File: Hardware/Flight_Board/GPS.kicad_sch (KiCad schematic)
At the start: 10 parts, among them U5 CAM-M8Q-0

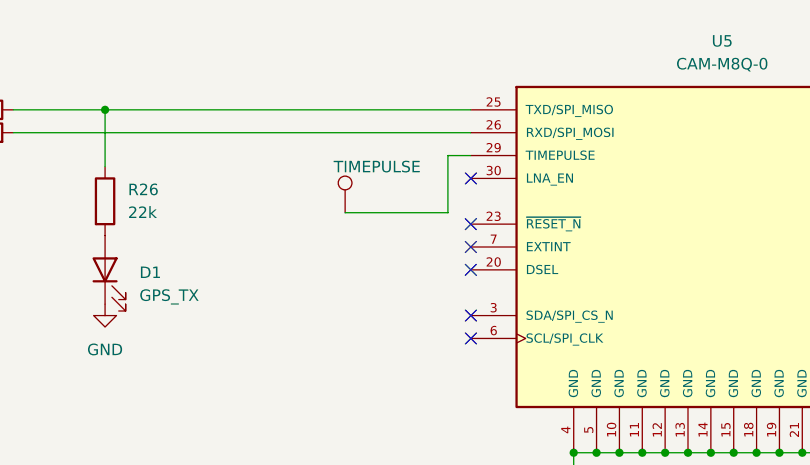
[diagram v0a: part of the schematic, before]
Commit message: fix some stuff and begin layout grouping
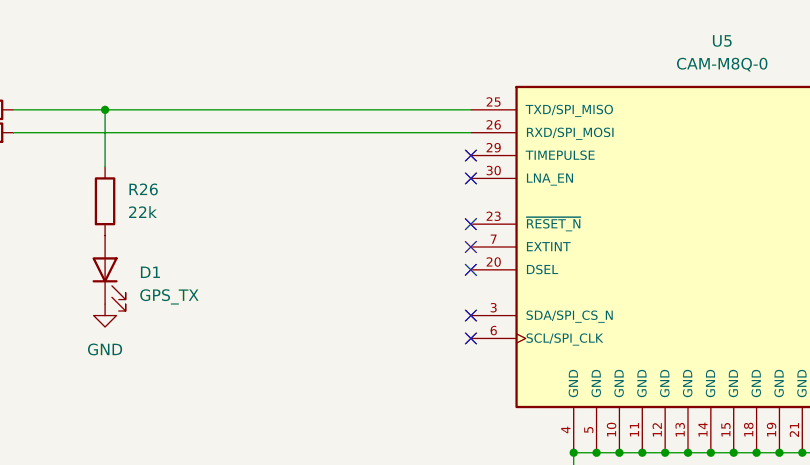
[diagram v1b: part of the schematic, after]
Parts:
- removed TP2: TIMEPULSE, TestPoint:TestPoint_THTPad_2.0x2.0mm_Drill1.0mm, symbol Connector:TestPoint
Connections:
- no-connect marks 8 -> 9
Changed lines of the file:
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@@
   (junction (at 177.8 100.33) (diameter 0) (color 0 0 0 0)
   )
+  (no_connect (at 146.05 67.31))
   (no_connect (at 146.05 77.47))
   (no_connect (at 146.05 69.85))
@@
     (stroke (width 0) (type default))
   )
-  (wire (pts (xy 132.08 73.66) (xy 143.51 73.66))
-    (stroke (width 0) (type default))
-  )
-  (wire (pts (xy 143.51 67.31) (xy 143.51 73.66))
-    (stroke (width 0) (type default))
-  )
   (wire (pts (xy 201.93 82.55) (xy 217.17 82.55))
     (stroke (width 0) (type default))
@@
   )
   (wire (pts (xy 201.93 62.23) (xy 212.09 62.23))
-    (stroke (width 0) (type default))
-  )
-  (wire (pts (xy 146.05 67.31) (xy 143.51 67.31))
     (stroke (width 0) (type default))
   )
@@
         )
       )
-    )
-  )
-  (symbol (lib_id "Connector:TestPoint") (at 132.08 73.66 0) (unit 1)
-    (in_bom yes) (on_board yes) (dnp no)
-    (property "Reference" "TP2" (at 137.16 70.358 90)
-      (effects (font (size 1.27 1.27)) hide)
-    )
-    (property "Value" "TIMEPULSE" (at 130.81 68.58 0)
-      (effects (font (size 1.27 1.27)) (justify left))
-    )
-    (property "Footprint" "TestPoint:TestPoint_THTPad_2.0x2.0mm_Drill1.0mm" (at 137.16 73.66 0)
-      (effects (font (size 1.27 1.27)) hide)
-    )
-    (property "Datasheet" "~" (at 137.16 73.66 0)
-      (effects (font (size 1.27 1.27)) hide)
-    )
-    (pin "1")
-    (instances
-      (project "Flight_Board"
-        (path "/e8eb85d5-f1ff-4500-895d-25b9ff5f6d36/bc23ea56-d50e-4ce7-856f-e38dfbe72971"
-          (reference "TP2") (unit 1)
-        )
-        (path "/e8eb85d5-f1ff-4500-895d-25b9ff5f6d36/43c0adf1-436b-4b66-9010-44cf9a79cc96"
-          (reference "TP3") (unit 1)
-        )
-        (path "/e8eb85d5-f1ff-4500-895d-25b9ff5f6d36/7c06db2a-34f5-45c0-9668-fbbbd940678c"
-          (reference "TP11") (unit 1)
-        )
-        (path "/e8eb85d5-f1ff-4500-895d-25b9ff5f6d36/52cae81a-54fe-42c0-9a19-be88b271d004"
-          (reference "TP15") (unit 1)
-        )
-      )

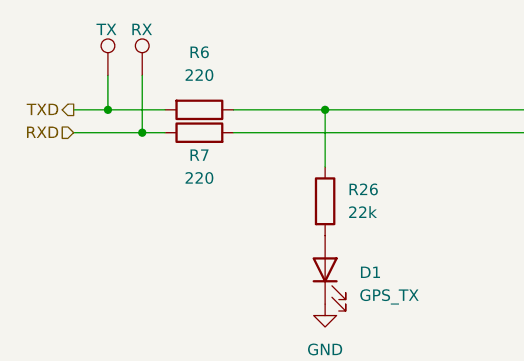
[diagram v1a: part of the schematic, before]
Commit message: initial placement on board, continue routing
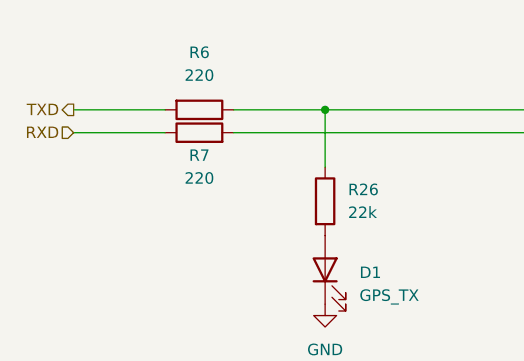
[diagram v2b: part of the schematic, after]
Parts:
- removed TP2: RX, TestPoint:TestPoint_THTPad_2.0x2.0mm_Drill1.0mm, symbol Connector:TestPoint
- removed TP2: TX, TestPoint:TestPoint_THTPad_2.0x2.0mm_Drill1.0mm, symbol Connector:TestPoint
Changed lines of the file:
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@@
 (kicad_sch (version 20230121) (generator eeschema)
   (paper "A4")
-  (junction (at 85.09 64.77) (diameter 0) (color 0 0 0 0)
-  )
   (junction (at 105.41 62.23) (diameter 0) (color 0 0 0 0)
   )
@@
   )
   (junction (at 167.64 100.33) (diameter 0) (color 0 0 0 0)
-  )
-  (junction (at 81.28 62.23) (diameter 0) (color 0 0 0 0)
   )
   (junction (at 175.26 100.33) (diameter 0) (color 0 0 0 0)
@@
     (stroke (width 0) (type default))
   )
-  (wire (pts (xy 85.09 58.42) (xy 85.09 64.77))
-    (stroke (width 0) (type default))
-  )
   (wire (pts (xy 212.09 62.23) (xy 212.09 64.77))
     (stroke (width 0) (type default))
@@
     (stroke (width 0) (type default))
   )
-  (wire (pts (xy 81.28 62.23) (xy 87.63 62.23))
-    (stroke (width 0) (type default))
-  )
   (wire (pts (xy 204.47 72.39) (xy 201.93 72.39))
     (stroke (width 0) (type default))
@@
     (stroke (width 0) (type default))
   )
-  (wire (pts (xy 77.47 64.77) (xy 85.09 64.77))
-    (stroke (width 0) (type default))
-  )
-  (wire (pts (xy 77.47 62.23) (xy 81.28 62.23))
-    (stroke (width 0) (type default))
-  )
-  (wire (pts (xy 85.09 64.77) (xy 87.63 64.77))
+  (wire (pts (xy 77.47 64.77) (xy 87.63 64.77))
+    (stroke (width 0) (type default))
+  )
+  (wire (pts (xy 77.47 62.23) (xy 87.63 62.23))
     (stroke (width 0) (type default))
   )
@@
   )
   (wire (pts (xy 160.02 100.33) (xy 162.56 100.33))
-    (stroke (width 0) (type default))
-  )
-  (wire (pts (xy 81.28 58.42) (xy 81.28 62.23))
     (stroke (width 0) (type default))
   )
@@
     )
   )
-  (symbol (lib_id "Connector:TestPoint") (at 85.09 58.42 0) (unit 1)
-    (in_bom yes) (on_board yes) (dnp no)
-    (property "Reference" "TP2" (at 90.17 55.118 90)
-      (effects (font (size 1.27 1.27)) hide)
-    )
-    (property "Value" "RX" (at 83.82 53.34 0)
-      (effects (font (size 1.27 1.27)) (justify left))
-    )
-    (property "Footprint" "TestPoint:TestPoint_THTPad_2.0x2.0mm_Drill1.0mm" (at 90.17 58.42 0)
-      (effects (font (size 1.27 1.27)) hide)
-    )
-    (property "Datasheet" "~" (at 90.17 58.42 0)
-      (effects (font (size 1.27 1.27)) hide)
-    )
-    (pin "1")
-    (instances
-      (project "Flight_Board"
-        (path "/e8eb85d5-f1ff-4500-895d-25b9ff5f6d36/bc23ea56-d50e-4ce7-856f-e38dfbe72971"
-          (reference "TP2") (unit 1)
-        )
-        (path "/e8eb85d5-f1ff-4500-895d-25b9ff5f6d36/43c0adf1-436b-4b66-9010-44cf9a79cc96"
-          (reference "TP3") (unit 1)
-        )
-        (path "/e8eb85d5-f1ff-4500-895d-25b9ff5f6d36/7c06db2a-34f5-45c0-9668-fbbbd940678c"
-          (reference "TP11") (unit 1)
-        )
-        (path "/e8eb85d5-f1ff-4500-895d-25b9ff5f6d36/52cae81a-54fe-42c0-9a19-be88b271d004"
-          (reference "TP14") (unit 1)
-        )
-      )
-    )
-  )
   (symbol (lib_id "power:GND") (at 157.48 102.87 0) (unit 1)
     (in_bom yes) (on_board yes) (dnp no) (fields_autoplaced)
@@
         )
       )
-    )
-  )
-  (symbol (lib_id "Connector:TestPoint") (at 81.28 58.42 0) (unit 1)
-    (in_bom yes) (on_board yes) (dnp no)
-    (property "Reference" "TP2" (at 86.36 55.118 90)
-      (effects (font (size 1.27 1.27)) hide)
-    )
-    (property "Value" "TX" (at 80.01 53.34 0)
-      (effects (font (size 1.27 1.27)) (justify left))
-    )
-    (property "Footprint" "TestPoint:TestPoint_THTPad_2.0x2.0mm_Drill1.0mm" (at 86.36 58.42 0)
-      (effects (font (size 1.27 1.27)) hide)
-    )
-    (property "Datasheet" "~" (at 86.36 58.42 0)
-      (effects (font (size 1.27 1.27)) hide)
-    )
-    (pin "1")
-    (instances
-      (project "Flight_Board"
-        (path "/e8eb85d5-f1ff-4500-895d-25b9ff5f6d36/bc23ea56-d50e-4ce7-856f-e38dfbe72971"
-          (reference "TP2") (unit 1)
-        )
-        (path "/e8eb85d5-f1ff-4500-895d-25b9ff5f6d36/43c0adf1-436b-4b66-9010-44cf9a79cc96"
-          (reference "TP3") (unit 1)
-        )
-        (path "/e8eb85d5-f1ff-4500-895d-25b9ff5f6d36/7c06db2a-34f5-45c0-9668-fbbbd940678c"
-          (reference "TP11") (unit 1)
-        )
-        (path "/e8eb85d5-f1ff-4500-895d-25b9ff5f6d36/52cae81a-54fe-42c0-9a19-be88b271d004"
-          (reference "TP13") (unit 1)
-        )
-      )

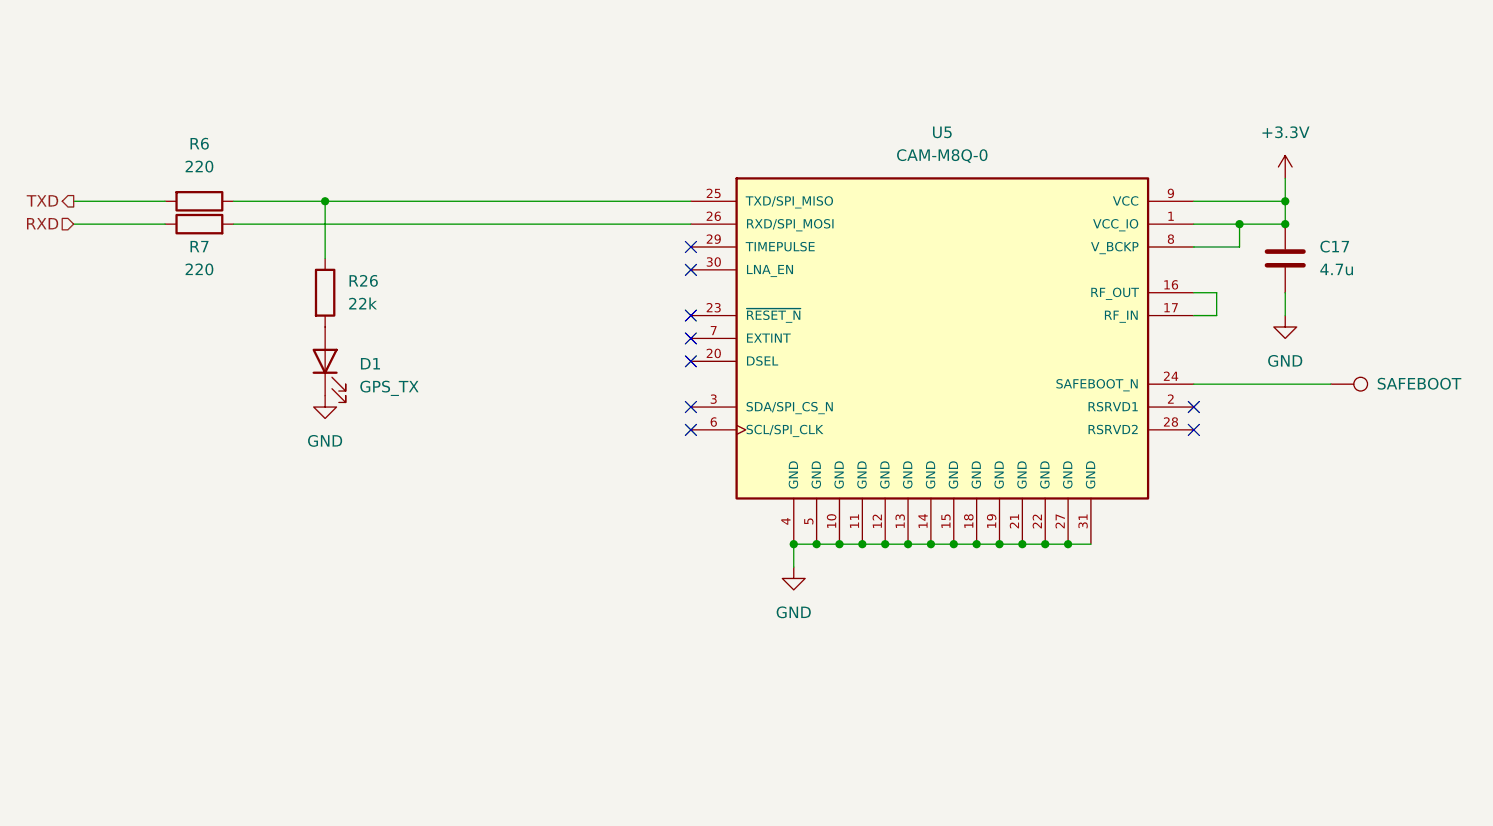
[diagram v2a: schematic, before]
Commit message: begin 4 layer board
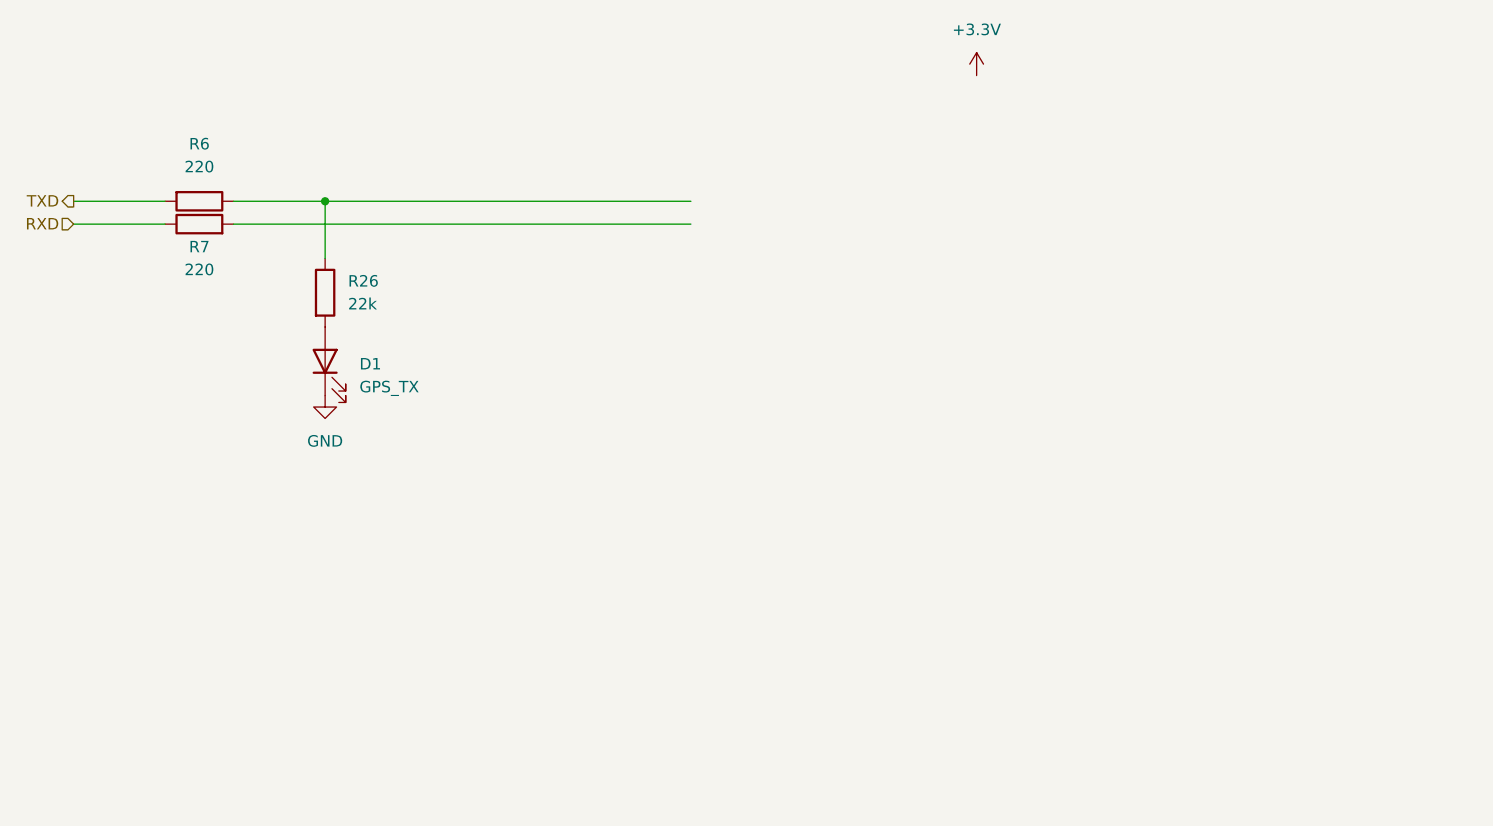
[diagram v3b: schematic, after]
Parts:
- removed C17: 4.7u, Capacitor_SMD:C_0603_1608Metric_Pad1.08x0.95mm_HandSolder, symbol Device:C
- removed TP1: SAFEBOOT, TestPoint:TestPoint_Pad_D1.0mm, symbol Connector:TestPoint
- removed U5: CAM-M8Q-0, Project:LCC100P960X1400X210-31N, symbol Project:CAM-M8Q-0
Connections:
- no-connect marks 9 -> 0

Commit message: initial route of 4-layer board
ouch
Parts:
- added C17: 1u, Capacitor_SMD:C_0603_1608Metric_Pad1.08x0.95mm_HandSolder, symbol Device:C
- added C18: 100n, Capacitor_SMD:C_0603_1608Metric_Pad1.08x0.95mm_HandSolder, symbol Device:C
- added FB2: FerriteBead, Resistor_SMD:R_0603_1608Metric_Pad0.98x0.95mm_HandSolder, symbol Device:FerriteBead
- added U5: FGPMMOPA6H, Project:FGPMMOPA6H, symbol Project:FGPMMOPA6H
- renumbered R7 to R10, R6 to R9
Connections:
- net +3.3V: now also FB2.1
- net GND: now also C17.2, C18.2, U5.12 (GND), U5.19 (GND), U5.3 (GND), U5.8 (GND)
- net at R26.1, R9.1: now also U5.9 (TX)
- net at R10.2: now also U5.10 (RX)
- new net: C17.1, C18.1, FB2.2, U5.1 (VCC)
- no-connect marks 0 -> 6
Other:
- moved on the sheet: D1, R10, R26, R9
